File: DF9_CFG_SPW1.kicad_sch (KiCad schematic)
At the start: 9 parts, among them J2 DF9-41P-1V32, J3 DF9-CFG-SPW1, U7 TPS3828-33DBVR

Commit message: SDRAM, bank5
last iteration of sdram. max optimization routing and space wise. Traced 2 frams to Bank 5. Fanout of bank 5 for DF9
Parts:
- R10, R11, R12, R13, R15: footprint Resistor_SMD:R_0603_1608Metric_Pad0.98x0.95mm_HandSolder -> Resistor_SMD:R_0402_1005Metric_Pad0.72x0.64mm_HandSolder
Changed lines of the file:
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@@
-		)
-	)
-	(label "RST_N"
-		(at 88.9 92.71 180)
-		(effects
-			(font
-				(size 1.27 1.27)
-			)
-			(justify right bottom)
 		)
 	)
@@
 			)
 			(justify right bottom)
+		)
+	)
+	(global_label "RST_N"
+		(shape input)
+		(at 88.9 92.71 0)
+		(fields_autoplaced yes)
+		(effects
+			(font
+				(size 1.27 1.27)
+			)
+			(justify left)
+		)
+		(property "Intersheetrefs" "${INTERSHEET_REFS}"
+			(at 97.6304 92.71 0)
+			(effects
+				(font
+					(size 1.27 1.27)
+				)
+				(justify left)
+				(hide yes)
+			)
 		)
 	)
@@
 			)
 		)
-		(property "Footprint" "Resistor_SMD:R_0603_1608Metric_Pad0.98x0.95mm_HandSolder"
+		(property "Footprint" "Resistor_SMD:R_0402_1005Metric_Pad0.72x0.64mm_HandSolder"
 			(at 60.96 60.96 0)
 			(effects
@@
 			)
 		)
-		(property "Footprint" "Resistor_SMD:R_0603_1608Metric_Pad0.98x0.95mm_HandSolder"
+		(property "Footprint" "Resistor_SMD:R_0402_1005Metric_Pad0.72x0.64mm_HandSolder"
 			(at 60.96 68.58 0)
 			(effects
@@
 			)
 		)
-		(property "Footprint" "Resistor_SMD:R_0603_1608Metric_Pad0.98x0.95mm_HandSolder"
+		(property "Footprint" "Resistor_SMD:R_0402_1005Metric_Pad0.72x0.64mm_HandSolder"
 			(at 106.68 34.29 0)
 			(effects
@@
 			)
 		)
-		(property "Footprint" "Resistor_SMD:R_0603_1608Metric_Pad0.98x0.95mm_HandSolder"
+		(property "Footprint" "Resistor_SMD:R_0402_1005Metric_Pad0.72x0.64mm_HandSolder"
 			(at 60.96 64.77 0)
 			(effects
@@
 			)
 		)
-		(property "Footprint" "Resistor_SMD:R_0603_1608Metric_Pad0.98x0.95mm_HandSolder"
+		(property "Footprint" "Resistor_SMD:R_0402_1005Metric_Pad0.72x0.64mm_HandSolder"
 			(at 53.34 34.29 0)
 			(effects

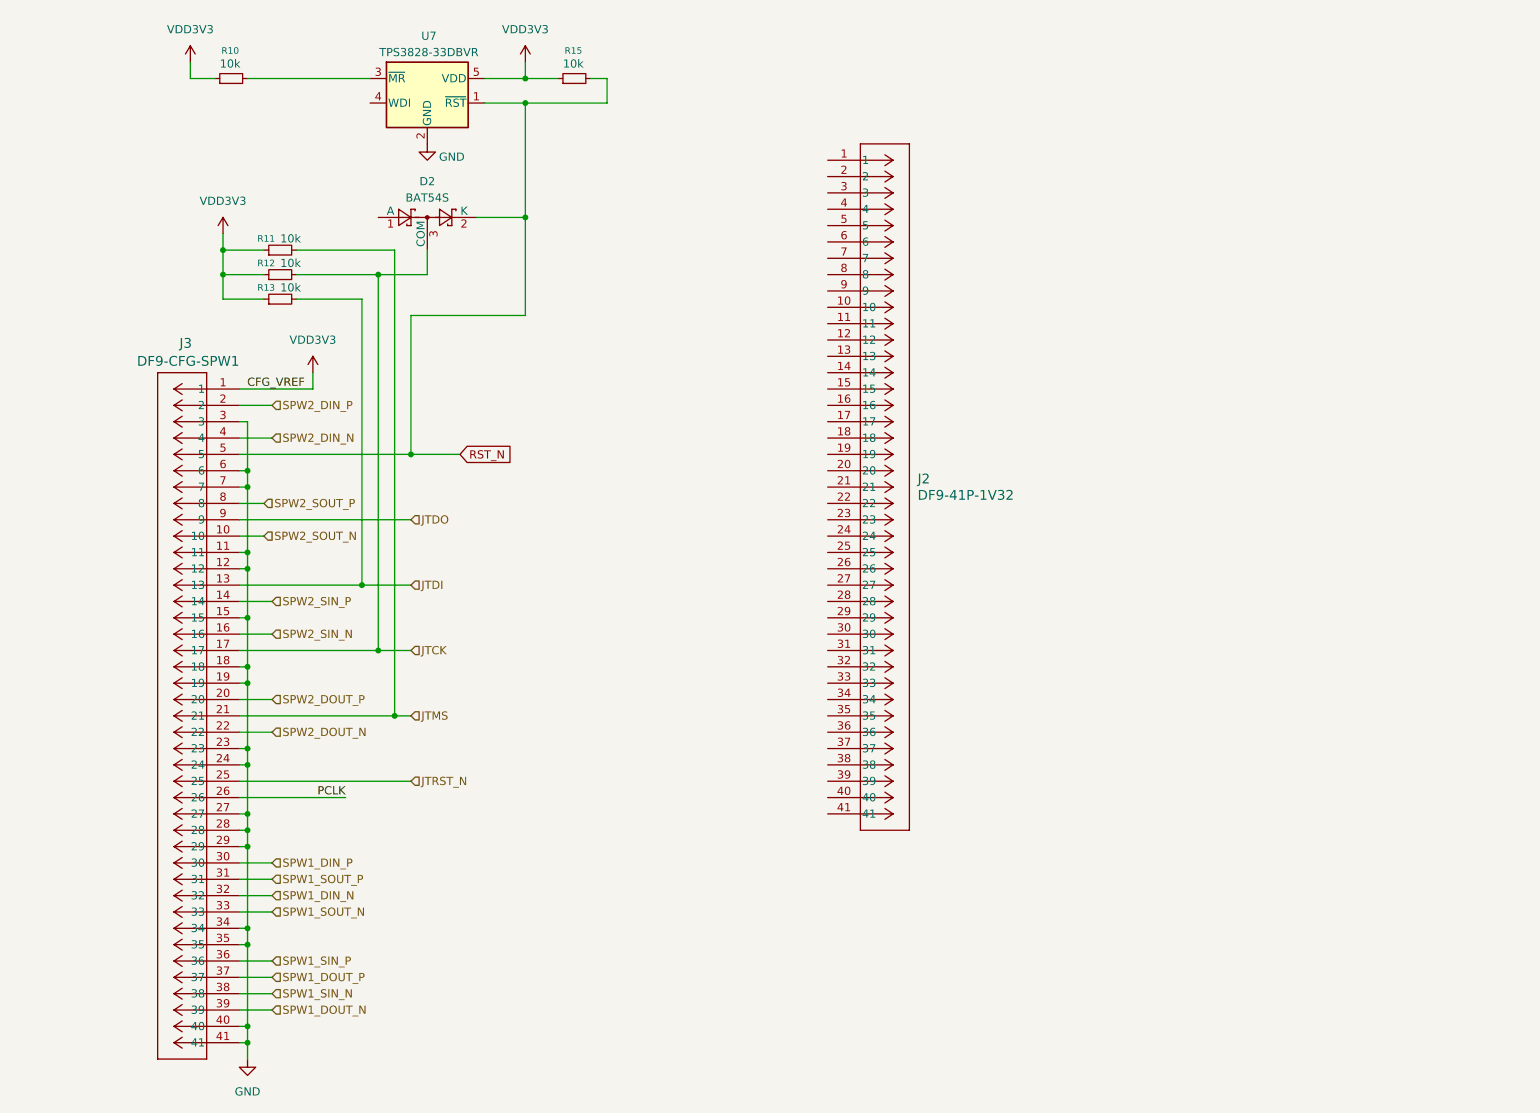
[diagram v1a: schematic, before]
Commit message: added MAX, picoblade, NPN
added the LDO (placement), added the picoblade connector for CFG and deleted one SPW out of 2 in the DF9.
added the NPN transistor (placed)
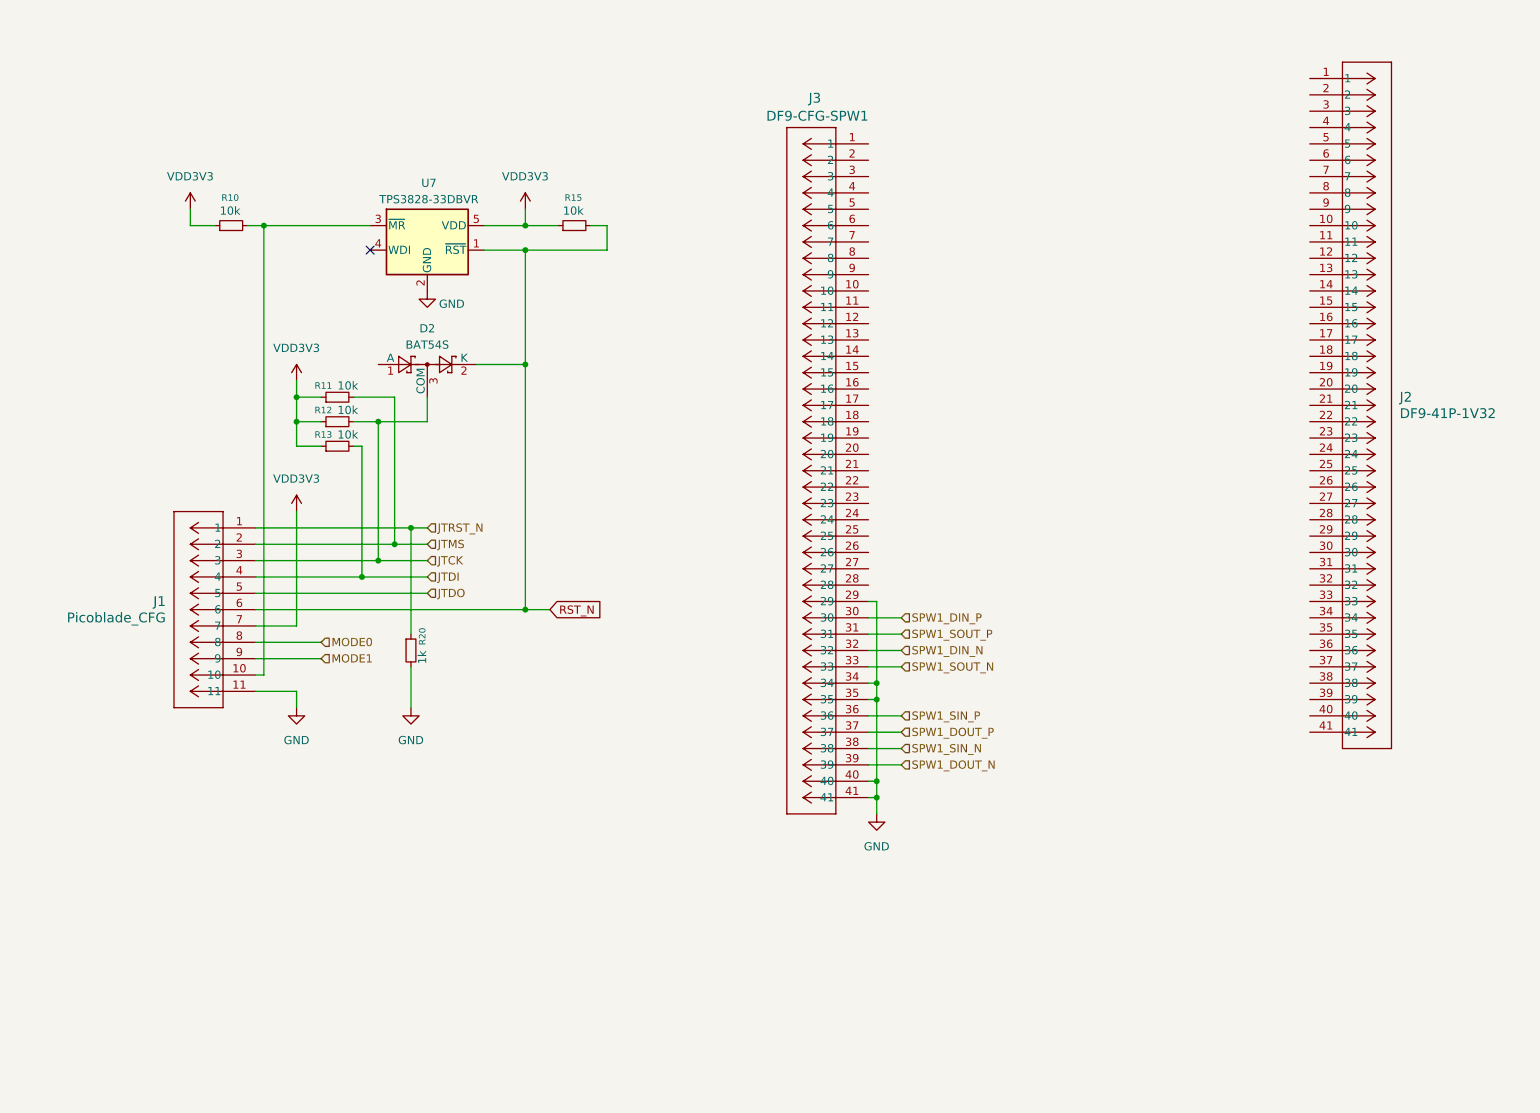
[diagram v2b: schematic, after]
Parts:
- added J1: Picoblade_CFG, DataHub_Footprints:CONN_532610001-SD_11_MOL, symbol Pico_Connector_11:532611171
- added R20: 1k, Resistor_SMD:R_0402_1005Metric_Pad0.72x0.64mm_HandSolder, symbol Device:R_Small
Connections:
- net GND: now also J1.11, R20.2; no longer J3.11, J3.12, J3.15, J3.18, J3.19, J3.23, J3.24, J3.27, J3.28, J3.3, J3.6, J3.7
- net JTCK: now also J1.3; no longer J3.17
- net JTDI: now also J1.4; no longer J3.13
- net JTDO: now also J1.5; no longer J3.9
- net JTMS: now also J1.2; no longer J3.21
- net JTRST_N: now also J1.1, R20.1; no longer J3.25
- net RST_N: now also J1.6; no longer J3.5
- net VDD3V3: now also J1.7; no longer J3.1
- net at R10.2, U7.3 (~{MR}): now also J1.10
- net PCLK: no longer names the net of J3.26
- net SPW2_DIN_N: no longer names the net of J3.4
- net SPW2_DIN_P: no longer names the net of J3.2
- net SPW2_DOUT_N: no longer names the net of J3.22
- net SPW2_DOUT_P: no longer names the net of J3.20
- net SPW2_SIN_N: no longer names the net of J3.16
- net SPW2_SIN_P: no longer names the net of J3.14
- net SPW2_SOUT_N: no longer names the net of J3.10
- net SPW2_SOUT_P: no longer names the net of J3.8
- new net MODE0: J1.8
- new net MODE1: J1.9
- no-connect marks 0 -> 1
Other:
- moved on the sheet: D2, J2, J3, R10, R11, R12, R13, R15, U7

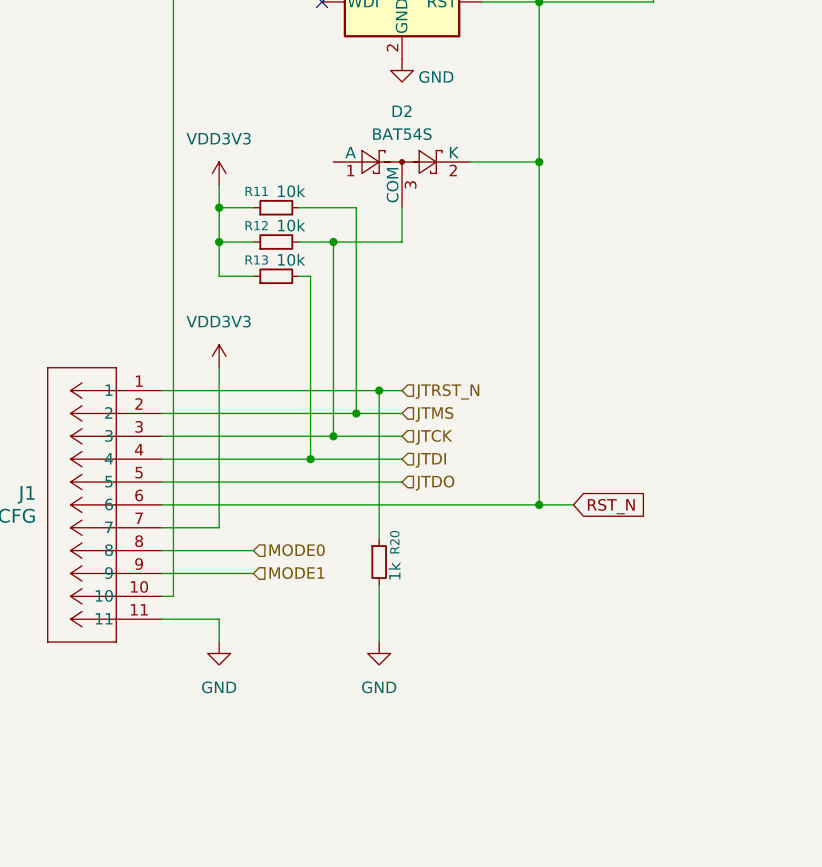
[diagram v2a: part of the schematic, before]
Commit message: full components, LEDS, changed edges
all components on pcb editor. added and  routed leds and 2 PLL. changed edges o have more space
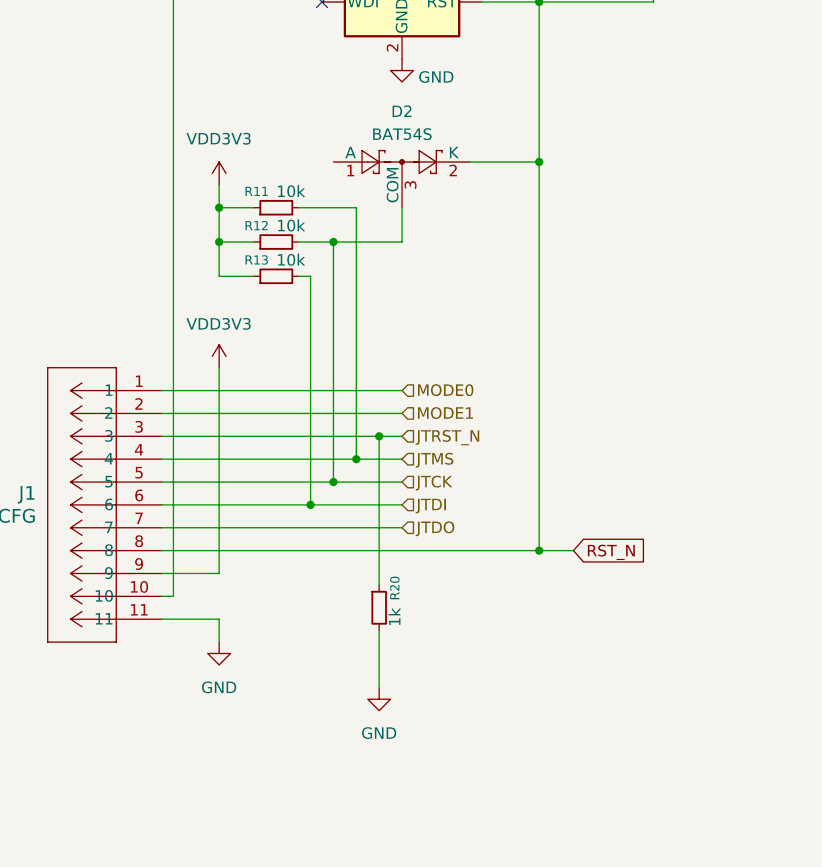
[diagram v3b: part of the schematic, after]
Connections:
- net JTCK: now also J1.5; no longer J1.3
- net JTDI: now also J1.6; no longer J1.4
- net JTDO: now also J1.7; no longer J1.5
- net JTMS: now also J1.4; no longer J1.2
- net JTRST_N: now also J1.3; no longer J1.1
- net MODE0: now also J1.1; no longer J1.8
- net MODE1: now also J1.2; no longer J1.9
- net RST_N: now also J1.8; no longer J1.6
- net VDD3V3: now also J1.9; no longer J1.7
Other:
- moved on the sheet: R20

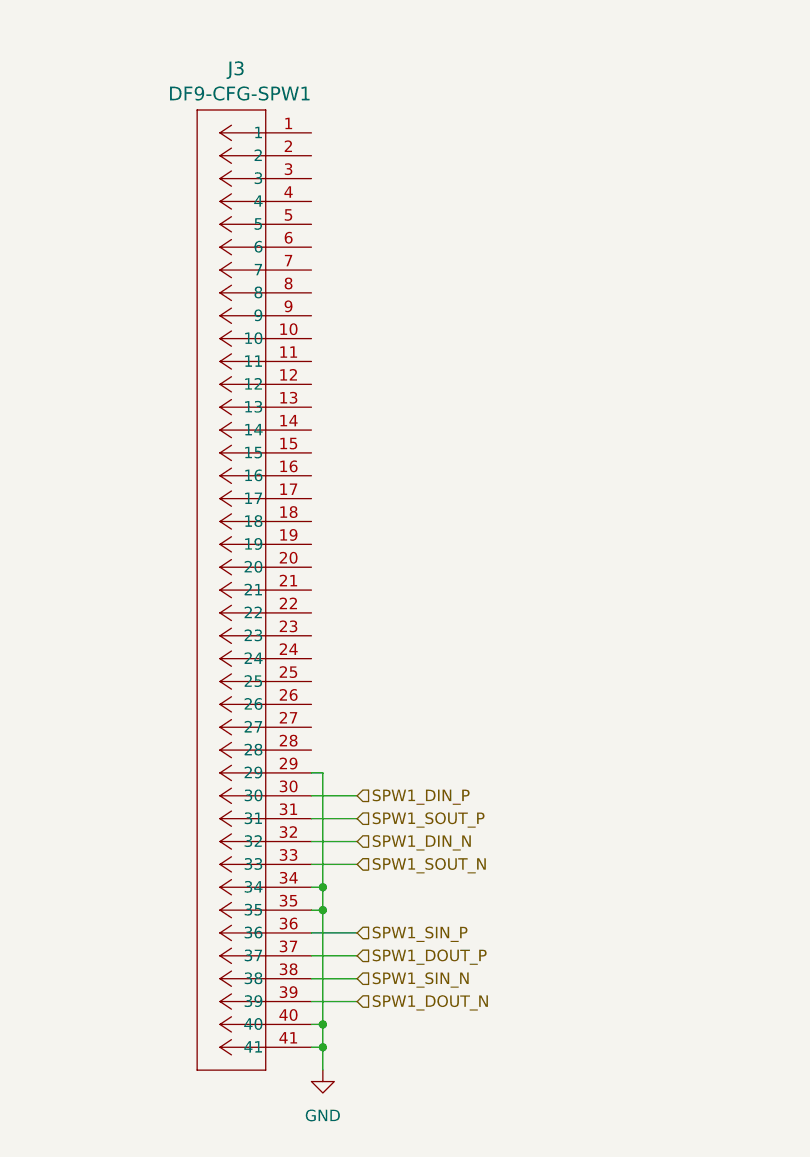
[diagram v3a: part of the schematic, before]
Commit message: SPW Bank0
completed SPW, rotated edges and adjusted dimensions to make the extra sdram bga fit. completed Bank 0 (still to route to connector). Started fanout of bga sdram
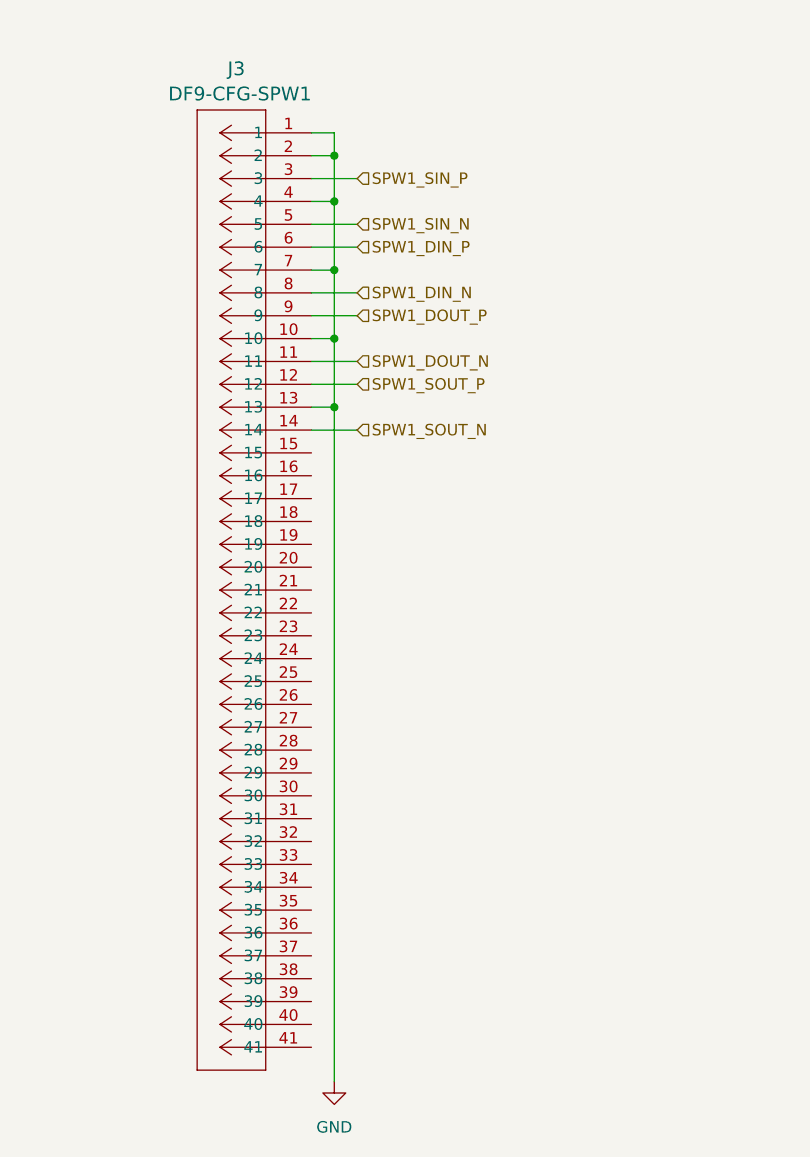
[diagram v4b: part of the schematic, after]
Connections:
- net GND: now also J3.1, J3.10, J3.13, J3.2, J3.4, J3.7; no longer J3.29, J3.34, J3.35, J3.40, J3.41
- net SPW1_DIN_N: now also J3.8; no longer J3.32
- net SPW1_DIN_P: now also J3.6; no longer J3.30
- net SPW1_DOUT_N: now also J3.11; no longer J3.39
- net SPW1_DOUT_P: now also J3.9; no longer J3.37
- net SPW1_SIN_N: now also J3.5; no longer J3.38
- net SPW1_SIN_P: now also J3.3; no longer J3.36
- net SPW1_SOUT_N: now also J3.14; no longer J3.33
- net SPW1_SOUT_P: now also J3.12; no longer J3.31
